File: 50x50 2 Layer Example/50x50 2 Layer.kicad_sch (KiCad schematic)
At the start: 76 parts, among them J1 Conn_01x02, J2 Conn_01x02, J3 USB_C_Receptacle_USB2.0_14P, J4 Conn_01x03, J5 Conn_01x04, SW1 SW_SPST, SW2 Reset, U1 RP2040, U2 W25Q128JVPIQ TR, U3 Voltage Regulator, Y1 12MHz

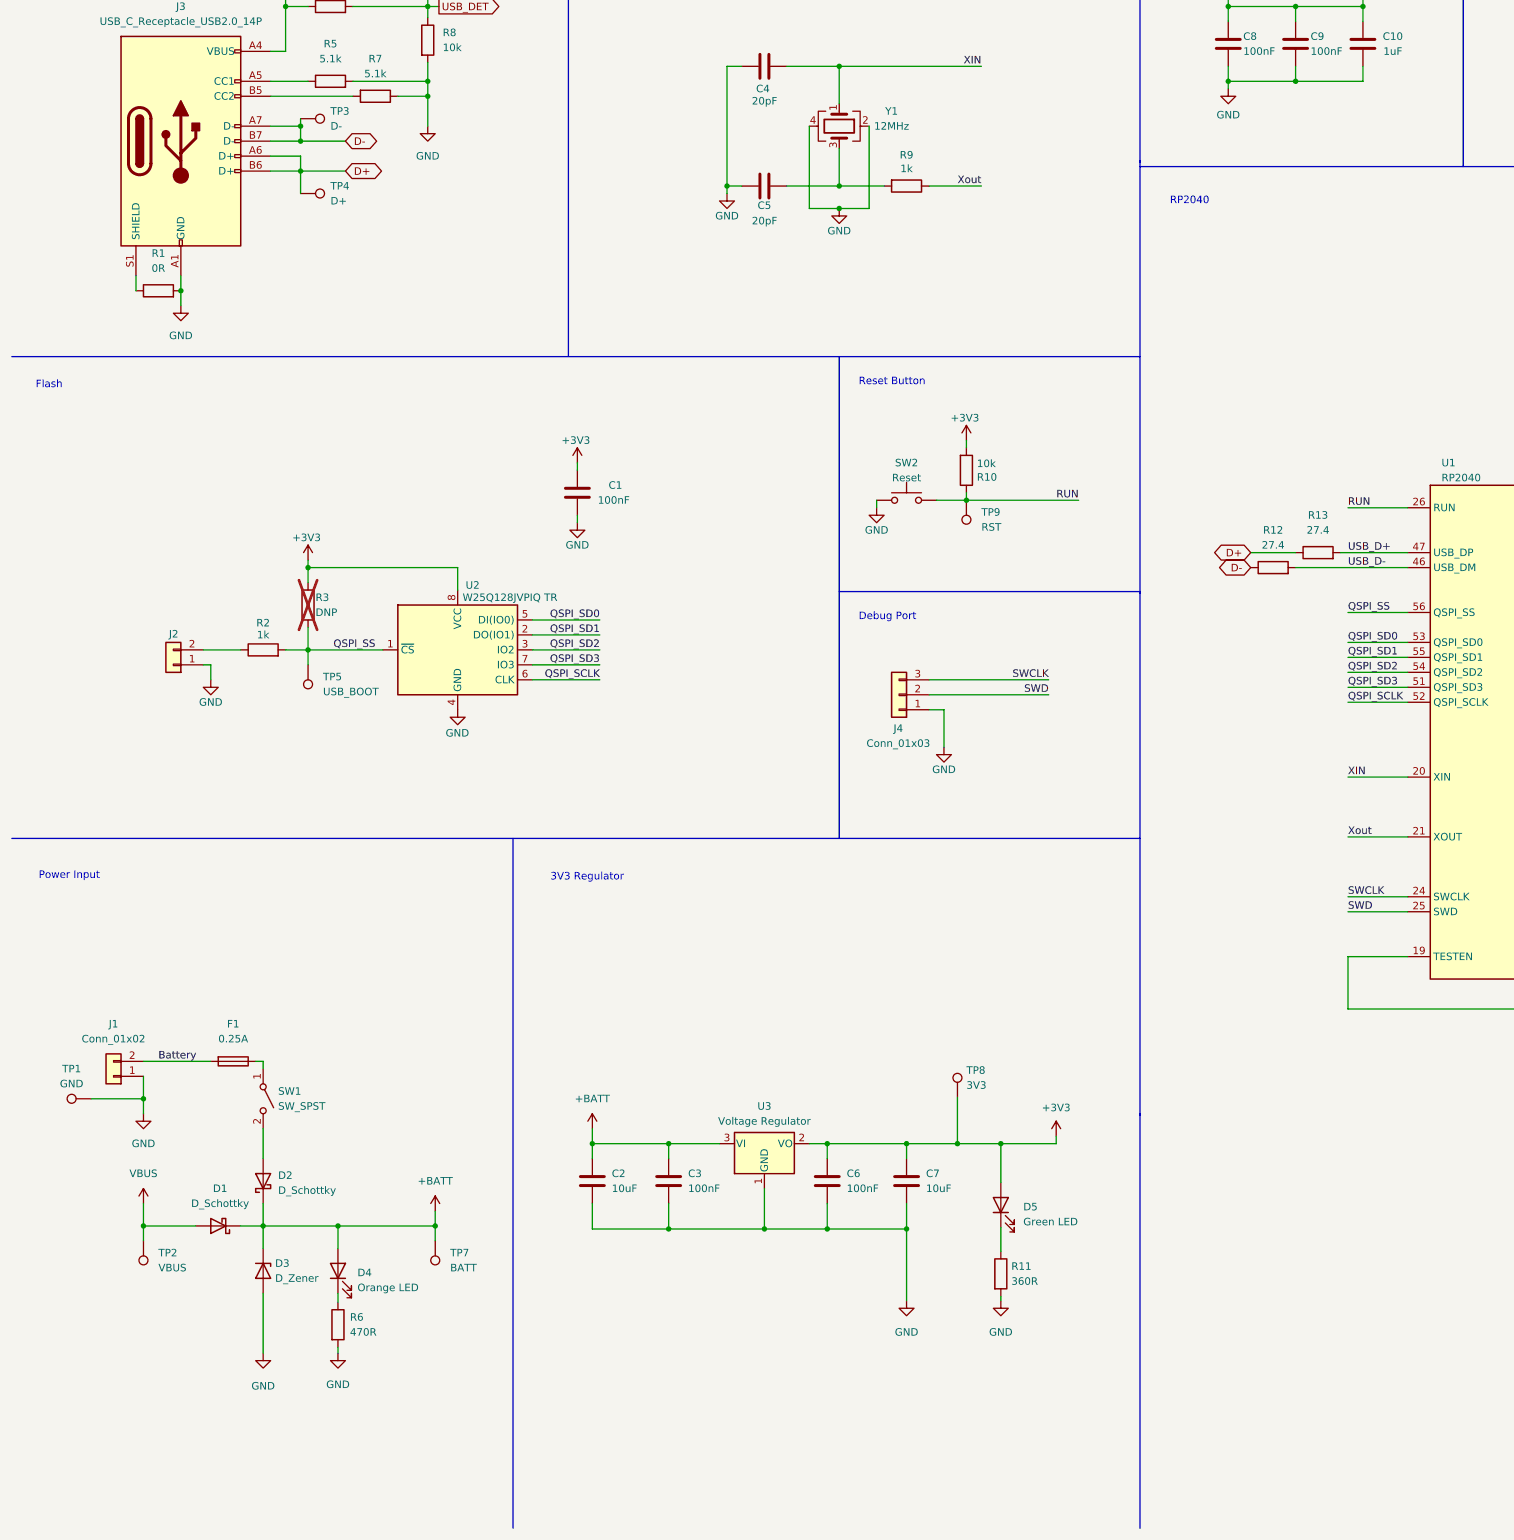
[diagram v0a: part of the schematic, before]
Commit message: Rework power input switching and protection
- Replace diode-OR with DPDT source select (VBUS/battery) plus
  separate on/off switch
- Add SMAJ8.5A TVS on the battery input
- Add per-source indicator LEDs, 820R battery / 560R USB
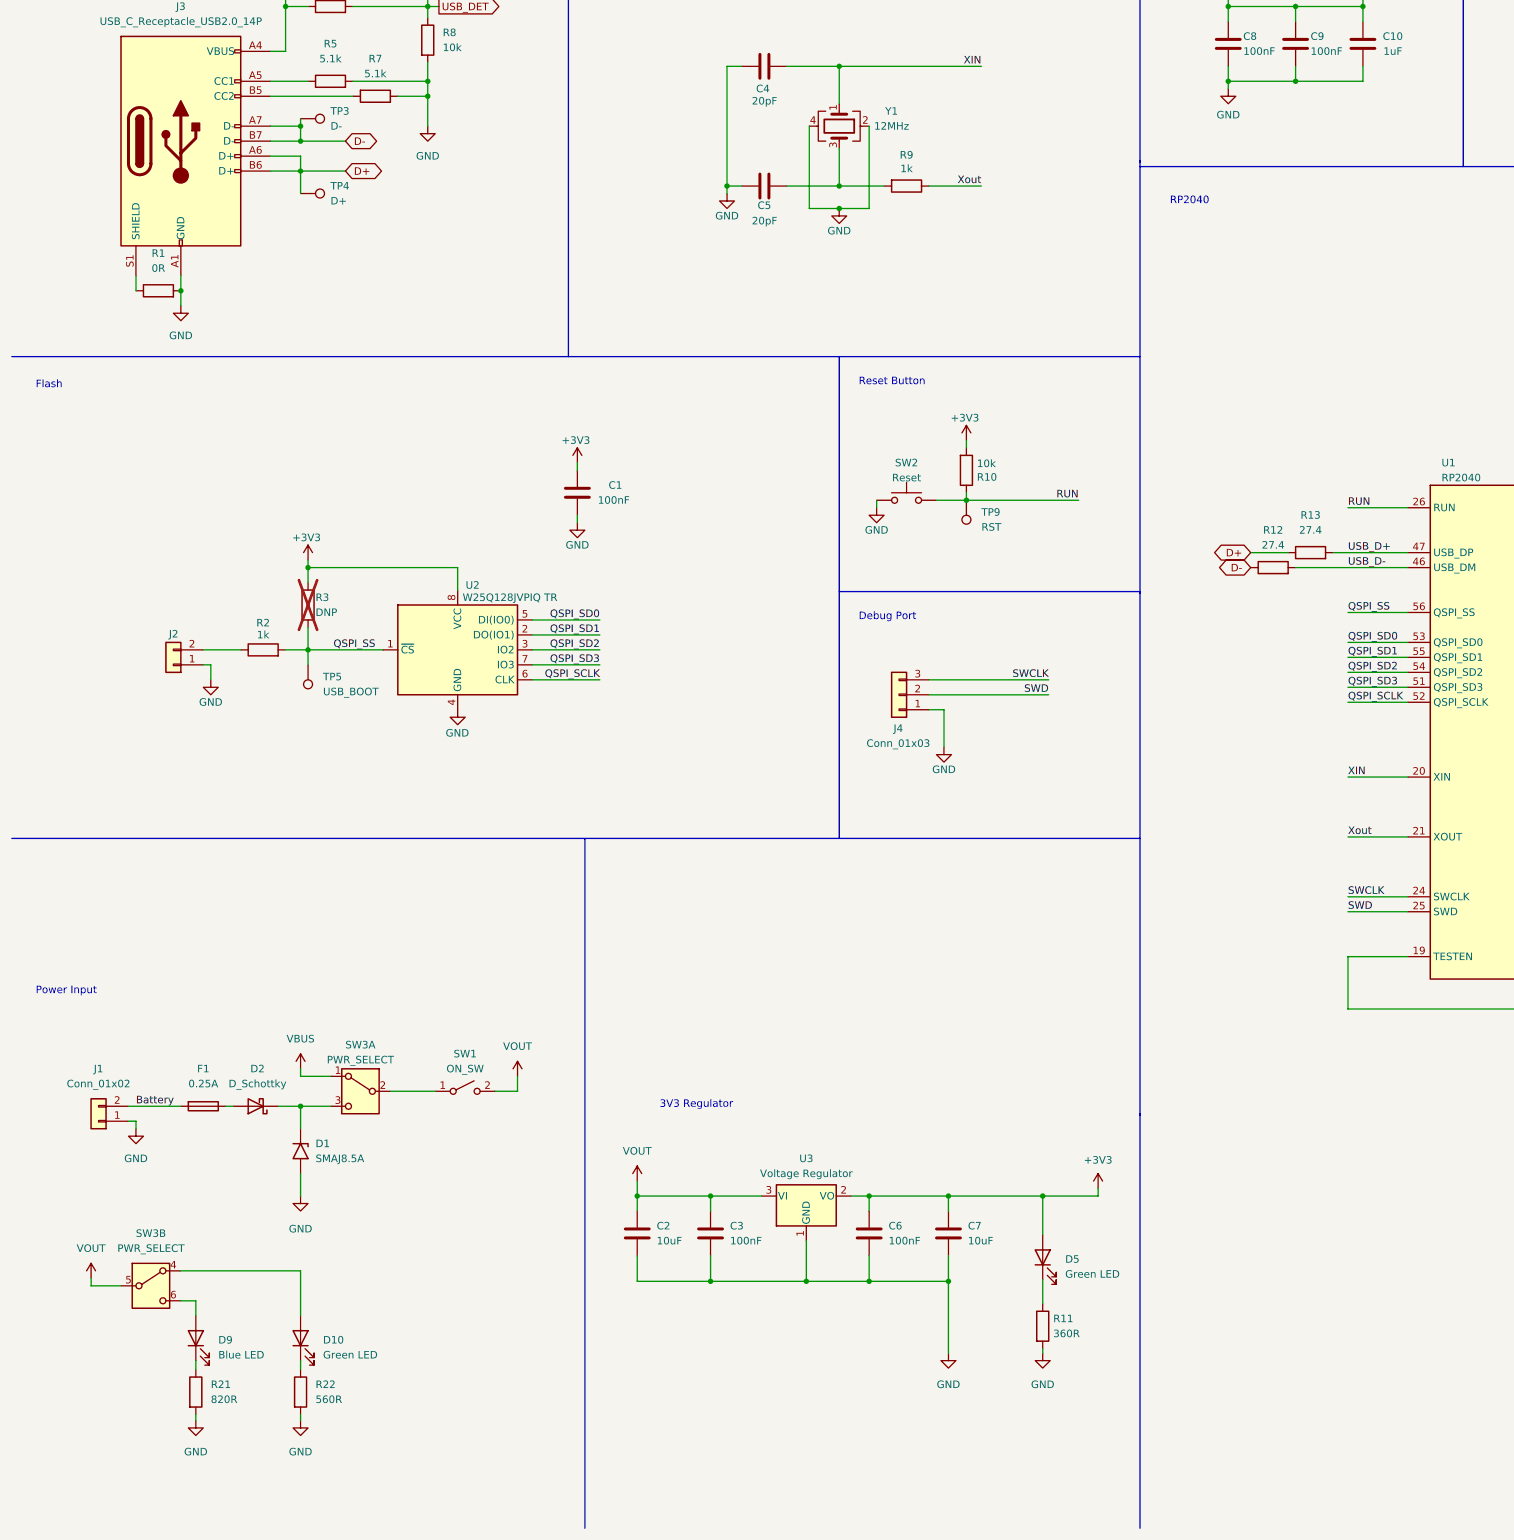
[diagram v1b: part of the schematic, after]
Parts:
- removed D1: D_Schottky, Diode_SMD:D_SMA, symbol Device:D_Schottky
- removed D3: D_Zener, Diode_SMD:D_SOD-123, symbol Device:D_Zener
- removed D4: Orange LED, LED_SMD:LED_0603_1608Metric, symbol Device:LED
- removed R6: 470R, Resistor_SMD:R_0805_2012Metric_Pad1.20x1.40mm_HandSolder, symbol Device:R
- removed TP1: GND, TestPoint:TestPoint_Pad_1.0x1.0mm, symbol Connector:TestPoint
- removed TP2: VBUS, TestPoint:TestPoint_Pad_1.0x1.0mm, symbol Connector:TestPoint
- removed TP7: BATT, TestPoint:TestPoint_Pad_1.0x1.0mm, symbol Connector:TestPoint
- removed TP8: 3V3, TestPoint:TestPoint_Pad_1.0x1.0mm, symbol Connector:TestPoint
- added D1: SMAJ8.5A, Diode_SMD:D_SMA, symbol Diode:SMAJ8.5A
- added D10: Green LED, LED_SMD:LED_0603_1608Metric, symbol Device:LED
- added D9: Blue LED, LED_SMD:LED_0603_1608Metric, symbol Device:LED
- added R21: 820R, Resistor_SMD:R_0805_2012Metric_Pad1.20x1.40mm_HandSolder, symbol Device:R
- added R22: 560R, Resistor_SMD:R_0805_2012Metric_Pad1.20x1.40mm_HandSolder, symbol Device:R
- added SW3: PWR_SELECT, symbol Switch:SW_DPDT_x2
- SW1: value SW_SPST -> ON_SW; footprint Connector_JST:JST_XH_B2B-XH-A_1x02_P2.50mm_Vertical -> (none); LCSC Part Number C158012 -> (none); MPN B2B-XH-A(LF)(SN) -> (none)
- U4: value ~ -> (none)
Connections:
- net GND: now also D1.2 (A2), R21.2, R22.2
- net VBUS: now also SW3.1 (A)
- net at D2.2 (A): now also F1.1; no longer SW1.2 (B)
- net at SW1.1 (A): now also SW3.2 (B); no longer F1.1
- net +BATT renamed VOUT
- net VOUT: now also SW1.2 (B), SW3.5 (B); no longer D2.1 (K)
- new net: D10.1 (K), R22.1
- new net: D10.2 (A), SW3.4 (A)
- new net: D1.1 (A1), D2.1 (K), SW3.3 (C)
- new net: D9.1 (K), R21.1
- new net: D9.2 (A), SW3.6 (C)
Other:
- moved on the sheet: C2, C3, C6, C7, D5, R11, R13, U3

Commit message: Updated Schematic to reflects changes to the 2026 Flight Computer
Updates:
MCU (RP2354A)
Voltage Regulator
Bypass/ Decoupling Capacitors
USB C
Crystal
Flash
Reset Button
Debug Port
LED
Buzzer
Status LEDs
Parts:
- removed C14, C15, C8: 100nF, Capacitor_SMD:C_0805_2012Metric_Pad1.18x1.45mm_HandSolder, symbol Device:C
- removed J2: Conn_01x02, Connector_PinHeader_2.54mm:PinHeader_1x02_P2.54mm_Vertical, symbol Connector_Generic:Conn_01x02
- removed R2: 1k, Resistor_SMD:R_0805_2012Metric_Pad1.20x1.40mm_HandSolder, symbol Device:R
- removed R3: DNP, Resistor_SMD:R_0805_2012Metric_Pad1.20x1.40mm_HandSolder, symbol Device:R
- removed TP10: 1V1, TestPoint:TestPoint_Pad_1.0x1.0mm, symbol Connector:TestPoint
- removed TP11: INT_1, TestPoint:TestPoint_Pad_1.0x1.0mm, symbol Connector:TestPoint
- removed TP12: I2C0_SCL, TestPoint:TestPoint_Pad_1.0x1.0mm, symbol Connector:TestPoint
- removed TP13: I2C1_SCL, TestPoint:TestPoint_Pad_1.0x1.0mm, symbol Connector:TestPoint
- removed TP14: I2C0_SDA, TestPoint:TestPoint_Pad_1.0x1.0mm, symbol Connector:TestPoint
- removed TP15: I2C1_SDA, TestPoint:TestPoint_Pad_1.0x1.0mm, symbol Connector:TestPoint
- removed TP3: D-, TestPoint:TestPoint_Pad_1.0x1.0mm, symbol Connector:TestPoint
- removed TP4: D+, TestPoint:TestPoint_Pad_1.0x1.0mm, symbol Connector:TestPoint
- removed TP5: USB_BOOT, TestPoint:TestPoint_Pad_1.0x1.0mm, symbol Connector:TestPoint
- removed TP6: USB_DET, TestPoint:TestPoint_Pad_1.0x1.0mm, symbol Connector:TestPoint
- removed TP9: RST, TestPoint:TestPoint_Pad_1.0x1.0mm, symbol Connector:TestPoint
- removed U1: RP2040, Package_DFN_QFN:QFN-56-1EP_7x7mm_P0.4mm_EP3.2x3.2mm, symbol MCU_RaspberryPi:RP2040
- removed U2: W25Q128JVPIQ TR, Package_SO:SOIC-8_5.23x5.23mm_P1.27mm, symbol Memory_Flash:W25Q128JVS
- removed U3: Voltage Regulator, Package_TO_SOT_SMD:SOT-223, symbol Regulator_Linear:AMS1117-3.3
- added BZ1: Buzzer, symbol Device:Buzzer
- added C11, C12: 4.7u, symbol Device:C
- added C16, C17, C18, C19: 100n, Capacitor_SMD:C_0805_2012Metric_Pad1.18x1.45mm_HandSolder, symbol Device:C
- added C2: 1u, symbol Device:C
- added D6, D7: WS2812B, LED_SMD:LED_WS2812B_PLCC4_5.0x5.0mm_P3.2mm, symbol LED:WS2812B
- added L1: 3.3u, symbol Device:L_Small
- added Q1: MMBT3904, Package_TO_SOT_SMD:SOT-23, symbol Transistor_BJT:MMBT3904
- added R12: 33, symbol Device:R
- added R15, R16: 1k, symbol Device:R
- added R7: 10k, symbol Device:R
- added U1: W25Q32JVSSIQ, Package_SO:SOIC-8_5.3x5.3mm_P1.27mm, symbol Memory_Flash:W25Q32JVSS
- added U2: USBLC6-2SC6, Package_TO_SOT_SMD:SOT-23-6, symbol Power_Protection:USBLC6-2SC6
- added U3: Voltage Regulator (MCP1755S-3302E/DB), Package_TO_SOT_SMD:SOT-23-3, symbol Regulator_Linear:MCP1754S-3302xCB
- added U4: RP2354A, Package_DFN_QFN:QFN-60-1EP_7x7mm_P0.4mm_EP3.4x3.4mm, symbol MCU_RaspberryPi:RP2354A
- C1, C9: value 100nF -> 100n; footprint Capacitor_SMD:C_0805_2012Metric_Pad1.18x1.45mm_HandSolder -> (none)
- C10: value 1uF -> 100n; footprint Capacitor_SMD:C_0805_2012Metric_Pad1.18x1.45mm_HandSolder -> (none); LCSC Part Number C28323 -> C28233; MPN CL21B105KBFNNNE -> CL21B104KCFNNNE
- C13: value 100nF -> 4.7u; footprint Capacitor_SMD:C_0805_2012Metric_Pad1.18x1.45mm_HandSolder -> (none); LCSC Part Number C28233 -> (none); MPN CL21B104KCFNNNE -> (none)
- C14: renamed from C11; value 100nF -> 100n
- C15: renamed from C12; value 100nF -> 100n
- C20: renamed from C16; value 1uF -> 10u
- C3: renamed from C2; value 10uF -> 22u
- C4: renamed from C3; value 100nF -> 100n
- C5: renamed from C6; value 100nF -> 100n
- C6: renamed from C7; value 10uF -> 22u
- C7: renamed from C4; value 20pF -> 15p
- C8: renamed from C5; value 20pF -> 15p
- R10: value 10k -> 1k; MPN 0805W8F1002T5E -> RC0805FR-074K7L
- R11: value 360R -> 360
- R13: renamed from R12; value 27.4 -> 27
- R14: renamed from R13; value 27.4 -> 27
- R2: renamed from R21; value 820R -> 820
- R21: renamed from R18; value 130 -> 80
- R22: renamed from R19; value 130 -> 80
- R23: renamed from R20; value 130 -> 80
- R3: renamed from R5; value 5.1k -> 5k1
- R4: renamed from R22; value 560R -> 560
- R5: renamed from R4; value 5.6k -> 5k6
- R6: renamed from R7; value 5.1k -> 5k1
- R9: MPN 0805W8F1001T5E -> RC0805FR-074K7L
- Y1: LCSC Part Number C50430 -> C20625731; MPN X322512MMB4SI -> ABM8-272-T3
- renumbered D9 to D1, D8 to D10, D1 to D3, D10 to D4, D6 to D8, D7 to D9, J3 to J2, J4 to J3, J5 to J4, R14 to R17, R15 to R18, R16 to R19, R17 to R20, SW3 to SW1, SW1 to SW2, SW2 to SW3, U4 to U5
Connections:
- net +1V1: now also C12.2, L1.1, U4.50 (VREG_FB); no longer C10.2, C9.1
- net +3V3: now also C1.1, C10.1, C9.1, BZ1.1 (+), C11.2, C16.1, C17.1, C18.1, C19.1, C2.1, D6.1 (VDD), D7.1 (VDD), R12.1, R16.1, R7.2, U1.3 (~{WP}/IO_{2}), U1.7 (~{HOLD}/~{RESET}/IO_{3}), U1.8 (VCC), U3.2 (VO), U4.1 (IOVDD), U4.44 (ADC_AVDD), U4.49 (VREG_VIN), U4.53 (USB_OTP_VDD), U4.54 (QSPI_IOVDD), U4.6 (DVDD); no longer C1.2, C13.1, R10.2
- net ADC_0: now also U4.40 (GPIO26/ADC0)
- net ADC_1: now also U4.41 (GPIO27/ADC1)
- net ADC_2: now also U4.42 (GPIO28/ADC2)
- net ADC_3: now also U4.43 (GPIO29/ADC3)
- net CLK_GPIN0: now also U4.32 (GPIO20)
- net CLK_GPOUT0: now also U4.33 (GPIO21)
- net D+: now also U2.4 (I/O2); no longer J2.A6 (D+), J2.B6 (D+)
- net D-: now also U2.6 (I/O1); no longer J2.A7 (D-), J2.B7 (D-)
- net GND: now also C1.2, C10.2, C13.1, J3.2 (Pin_2), R10.2, C11.1, C12.1, C16.2, C17.2, C18.2, C19.2, C2.2, D6.3 (VSS), D7.3 (VSS), Q1.2 (E), U1.4 (GND), U2.2 (GND), U3.1 (GND), U4.47 (VREG_PGND), U4.61 (GND); no longer C1.1, C10.1, C13.2, J3.1 (Pin_1), SW3.1
- net GPIO_3: now also U4.5 (GPIO3)
- net GPIO_4: now also U4.7 (GPIO4)
- net GPIO_5: now also U4.8 (GPIO5)
- net GPIO_6: now also U4.9 (GPIO6)
- net GPIO_7: now also U4.10 (GPIO7)
- net I2C0_SCL: now also U4.37 (GPIO25)
- net I2C0_SDA: now also U4.36 (GPIO24)
- net I2C1_SCL: now also U4.35 (GPIO23)
- net I2C1_SDA: now also U4.34 (GPIO22)
- net INT_1: now also U4.12 (GPIO8)
- net LED_GREEN: now also U4.15 (GPIO11)
- net LED_RED: now also U4.13 (GPIO9)
- net LED_YELLOW: now also U4.14 (GPIO10)
- net RUN: now also U4.26 (RUN); no longer R10.1
- net SPI0_CSn: now also U4.28 (GPIO17)
- net SPI0_MISO: now also U4.27 (GPIO16)
- net SPI0_MOSI: now also U4.31 (GPIO19)
- net SPI0_SCK: now also U4.29 (GPIO18)
- net SPI1_CSn: now also R7.1, U1.1 (~{CS}), U4.17 (GPIO13)
- net SPI1_MISO: now also U1.2 (DO/IO_{1}), U4.16 (GPIO12)
- net SPI1_MOSI: now also U1.5 (DI/IO_{0}), U4.19 (GPIO15)
- net SPI1_SCK: now also U1.6 (CLK), U4.18 (GPIO14)
- net SWCLK: now also J3.1 (Pin_1), U4.24 (SWCLK); no longer J3.3 (Pin_3)
- net SWD: now also J3.3 (Pin_3), U4.25 (SWDIO); no longer J3.2 (Pin_2)
- net USB_D+: now also U4.52 (USB_DP)
- net USB_D-: now also U4.51 (USB_DM)
- net USB_DET: now also U4.2 (GPIO0)
- net VBUS: now also U2.5 (VBUS)
- net VOUT: now also U3.3 (VI)
- net XIN: now also U4.21 (XIN)
- net Xout renamed XOUT
- net XOUT: now also U4.22 (XOUT)
- new net: C13.2, R12.2, U4.46 (VREG_AVDD)
- new net: Q1.1 (B), R15.1
- new net: R10.1, SW3.1
- new net: BZ1.2 (-), Q1.3 (C), R16.2
- new net: D6.2 (DOUT), D7.4 (DIN)
- new net: U4.11 (IOVDD), U4.20 (IOVDD), U4.30 (IOVDD), U4.38 (IOVDD), U4.45 (IOVDD)
- new net: U4.23 (DVDD), U4.39 (DVDD)
- new net: L1.2, U4.48 (VREG_LX)
- new net: J2.A6 (D+), J2.B6 (D+), U2.3 (I/O2)
- new net: J2.A7 (D-), J2.B7 (D-), U2.1 (I/O1)
- new net BUZZER: R15.2, U4.4 (GPIO2)
- new net LED_RGB: D6.4 (DIN), U4.3 (GPIO1)
- no-connect marks 0 -> 7
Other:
- note added: "Buzzer"
- note added: "LED"
- note added: "RP2354A"
- note removed: "Internal 1.1v regulator bypass"
- note removed: "RP2040"
- moved on the sheet: C14, C15, C20, C3, C4, C5, C6, D1, D2, D3, D4, D5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

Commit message: Minor changes to Schematic
Adjusted green sections and added Footprints
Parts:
- C1, C10, C11, C12, C13, C2, C9: footprint (none) -> Capacitor_SMD:C_0805_2012Metric_Pad1.18x1.45mm_HandSolder
- R12, R15, R16, R7: footprint (none) -> Resistor_SMD:R_0805_2012Metric_Pad1.20x1.40mm_HandSolder
- U5: value (none) -> Sensor Board
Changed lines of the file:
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@@
 	)
 	(rectangle
+		(start 351.79 218.44)
+		(end 397.51 247.65)
+		(stroke
+			(width 0)
+			(type default)
+			(color 0 255 0 1)
+		)
+		(fill
+			(type none)
+		)
+	)
+	(rectangle
 		(start 49.53 95.25)
 		(end 114.3 154.94)
@@
 			)
 		)
-		(property "Footprint" ""
+		(property "Footprint" "Resistor_SMD:R_0805_2012Metric_Pad1.20x1.40mm_HandSolder"
 			(at 229.87 144.018 90)
 			(hide yes)
@@
 			)
 		)
-		(property "Footprint" ""
+		(property "Footprint" "Capacitor_SMD:C_0805_2012Metric_Pad1.18x1.45mm_HandSolder"
 			(at 217.4748 157.48 0)
 			(hide yes)
@@
 			)
 		)
-		(property "Footprint" ""
+		(property "Footprint" "Capacitor_SMD:C_0805_2012Metric_Pad1.18x1.45mm_HandSolder"
 			(at 245.4148 31.75 0)
 			(hide yes)
@@
 			)
 		)
-		(property "Footprint" ""
+		(property "Footprint" "Resistor_SMD:R_0805_2012Metric_Pad1.20x1.40mm_HandSolder"
 			(at 254 102.108 90)
 			(hide yes)
@@
 			)
 		)
-		(property "Footprint" ""
+		(property "Footprint" "Resistor_SMD:R_0805_2012Metric_Pad1.20x1.40mm_HandSolder"
 			(at 265.938 87.63 90)
 			(hide yes)
@@
 			)
 		)
-		(property "Footprint" ""
+		(property "Footprint" "Capacitor_SMD:C_0805_2012Metric_Pad1.18x1.45mm_HandSolder"
 			(at 249.2248 143.51 0)
 			(hide yes)
@@
 			)
 		)
-		(property "Footprint" ""
+		(property "Footprint" "Capacitor_SMD:C_0805_2012Metric_Pad1.18x1.45mm_HandSolder"
 			(at 101.2952 115.57 0)
 			(hide yes)
@@
 			)
 		)
-		(property "Footprint" ""
+		(property "Footprint" "Capacitor_SMD:C_0805_2012Metric_Pad1.18x1.45mm_HandSolder"
 			(at 222.5548 33.02 0)
 			(hide yes)
@@
 			)
 		)
-		(property "Footprint" ""
+		(property "Footprint" "Resistor_SMD:R_0805_2012Metric_Pad1.20x1.40mm_HandSolder"
 			(at 72.898 116.84 90)
 			(hide yes)
@@
 			)
 		)
-		(property "Value" ""
+		(property "Value" "Sensor Board"
 			(at 381 181.61 0)
 			(show_name no)
@@
 			)
 		)
-		(property "Footprint" ""
+		(property "Footprint" "Capacitor_SMD:C_0805_2012Metric_Pad1.18x1.45mm_HandSolder"
 			(at 88.5952 115.57 0)
 			(hide yes)
@@
 			)
 		)
-		(property "Footprint" ""
+		(property "Footprint" "Capacitor_SMD:C_0805_2012Metric_Pad1.18x1.45mm_HandSolder"
 			(at 227.6348 157.48 0)
 			(hide yes)
